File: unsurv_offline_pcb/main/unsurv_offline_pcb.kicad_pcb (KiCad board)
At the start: 4 copper layers, 35 x 50 mm, 51 parts, among them J1 USB_B_Micro, J2 S2B-PH-SM4-TB_LF__SN_, J3 1.27mm_female_connector, Q1 Q_PMOS_GSD, Q2 UMH3N, SW1 SW_DIP_x01, U1 MCP73831-2-OT, U2 APX803L20, U3 AP2112K-3.3, U4 MPU-6050_NRND, U5 ESP32-WROOM-32, U6 CAM-M8C-0-10, U7 CH340G

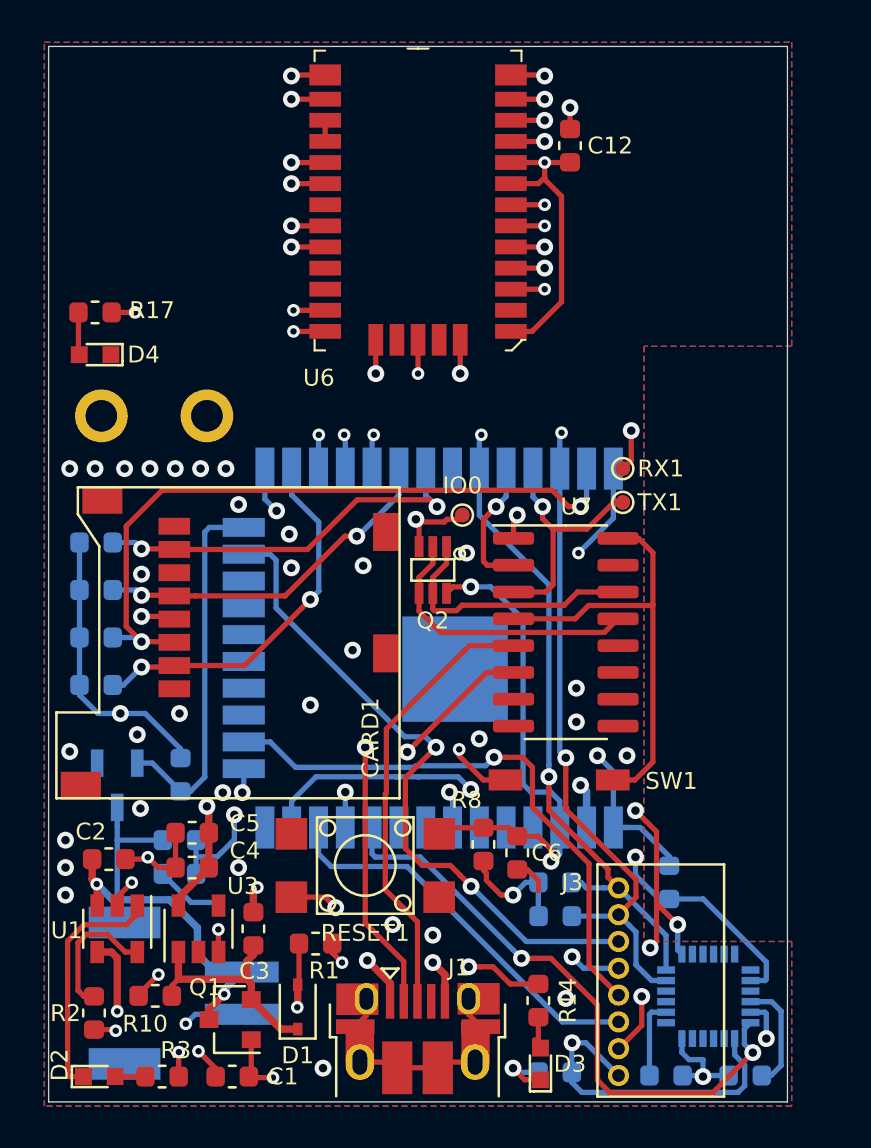
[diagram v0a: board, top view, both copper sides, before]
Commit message: added 3x2 pads for pogo pins
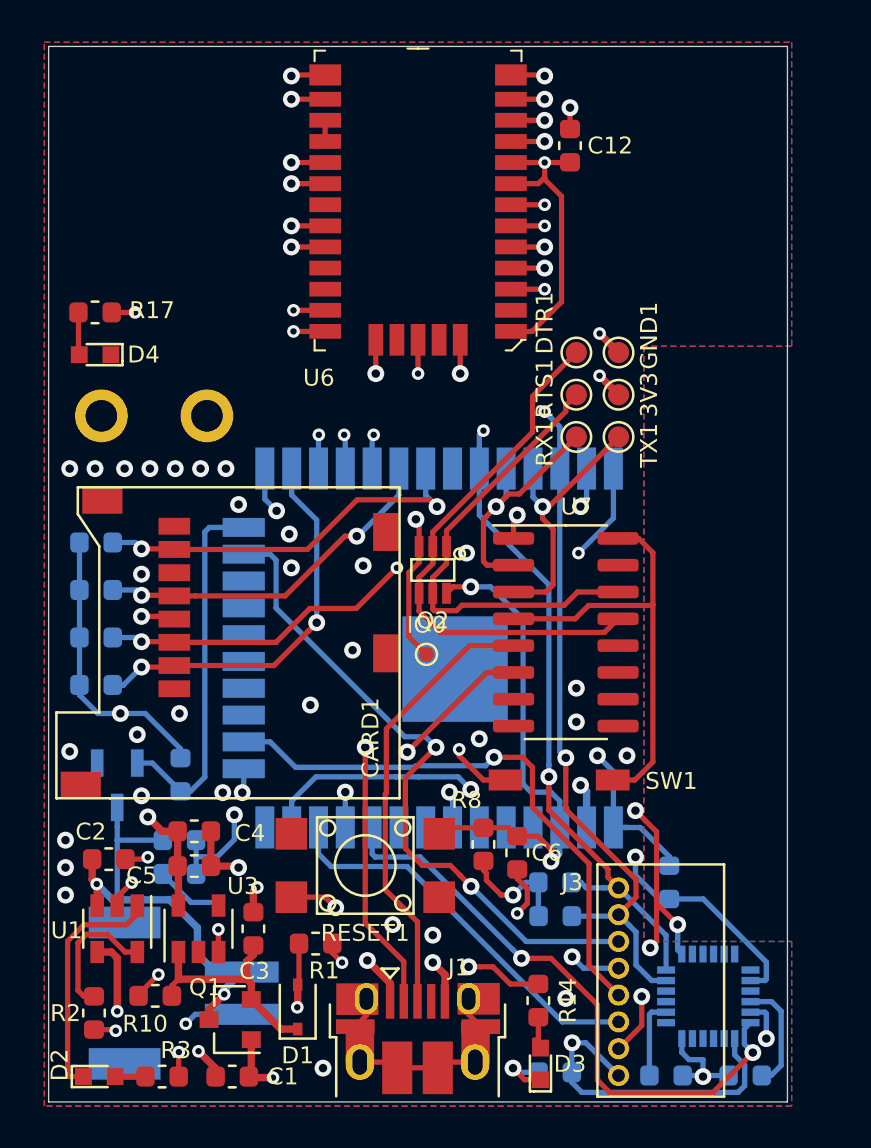
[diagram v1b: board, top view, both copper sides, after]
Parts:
- added 3V3: TestPoint, TestPoint:TestPoint_Pad_D1.0mm, F.Cu at (102.0, 91.5)
- added DTR1: TestPoint, TestPoint:TestPoint_Pad_D1.0mm, F.Cu at (100.0, 89.5)
- added GND1: TestPoint, TestPoint:TestPoint_Pad_D1.0mm, F.Cu at (102.0, 89.5)
- added RTS1: TestPoint, TestPoint:TestPoint_Pad_D1.0mm, F.Cu at (100.0, 91.5)
- RX1, TX1: footprint unsurv_offline_pcb_footprints:TestPoint_Pad_D0.7mm -> TestPoint:TestPoint_Pad_D1.0mm
- moved IO0 6.82 mm to (92.9, 103.8)
- moved TX1 3.11 mm to (102.0, 93.5), turned to 270 degrees
- moved RX1 2.66 mm to (100.0, 93.5), turned to 90 degrees
- moved C4 1.72 mm to (81.9, 112.2), turned to 180 degrees
- moved C5 1.58 mm to (81.9, 113.8), turned to 180 degrees
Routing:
- net DTR: track 13.4 -> 25.4 mm
- net RTS: track 12.4 -> 22.1 mm
- net 23: track 33.3 -> 26.8 mm, vias 2 -> 3
- net SDA: track 46.7 -> 41.1 mm
- net RX0: track 16.2 -> 11.5 mm, vias 2 -> 1
- net 5: track 30.0 -> 25.6 mm
- net SCL: track 47.4 -> 43.8 mm
- net 0: track 12.7 -> 16.0 mm
- net GND: track 84.4 -> 86.1 mm, vias 67 -> 69
- net +3V3: track 72.1 -> 73.6 mm, vias 9 -> 10
- net TX0: track 11.9 -> 12.9 mm
- net 4: track 17.9 -> 18.7 mm

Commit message: added RF430CL330H to pcb
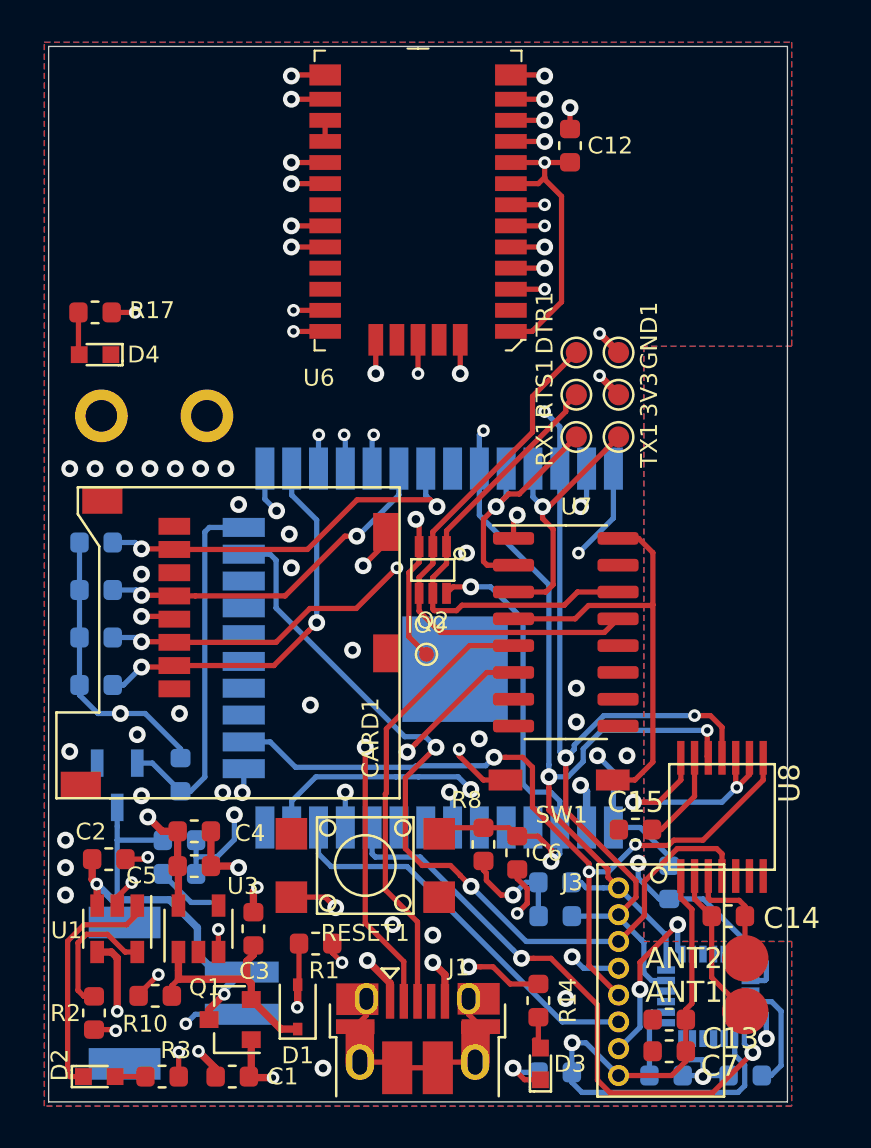
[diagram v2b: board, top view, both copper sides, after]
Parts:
- added ANT1: TestPoint, unsurv_offline_pcb_footprints:PogoPin_2_2mm_circular, F.Cu at (108.0, 120.7)
- added ANT2: TestPoint, unsurv_offline_pcb_footprints:PogoPin_2_2mm_circular, F.Cu at (108.0, 118.2)
- added C13: 1yF, Capacitor_SMD:C_0603_1608Metric, F.Cu at (104.4, 121.1)
- added C14: 10pF, Capacitor_SMD:C_0603_1608Metric, F.Cu at (107.2, 116.2)
- added C15: 470nF, Capacitor_SMD:C_0603_1608Metric, F.Cu at (102.8, 112.1)
- added C7: 0.1yF, Capacitor_SMD:C_0603_1608Metric, F.Cu at (104.4, 122.6)
- added U8: RF430CL330H, unsurv_offline_pcb_footprints:RF430CL330H, F.Cu at (106.9, 111.5)
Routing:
- net +3V3: track 73.6 -> 86.0 mm
- net 13: track 27.1 -> 38.2 mm, vias 1 -> 3
- net SDA: track 41.1 -> 51.3 mm, vias 3 -> 4
- net SCL: track 43.8 -> 53.8 mm, vias 3 -> 4
- net GND: track 86.1 -> 95.8 mm
- net 15: track 31.6 -> 40.4 mm
- net ANT1: track 0.00 -> 7.39 mm
- net ANT2: track 0.00 -> 5.42 mm
- net Net-(C15-Pad1): track 0.00 -> 4.49 mm

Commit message: bottom case
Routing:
- net GND: track 95.8 -> 101.1 mm, vias 69 -> 70
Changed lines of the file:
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@@
     (thickness 1.6)
     (drawings 4)
-    (tracks 761)
+    (tracks 768)
     (zones 0)
     (modules 62)
@@
   (module unsurv_offline_pcb_footprints:RF430CL330H (layer F.Cu)
     (at 106.9 111.5 90)
-    (fp_text reference U8 (at 1.6 3.2 90) (layer F.SilkS)
-      (effects (font (size 1 1) (thickness 0.15)))
+    (fp_text reference U8 (at 4.6 1.2 180) (layer F.SilkS)
+      (effects (font (size 0.8 0.8) (thickness 0.1)))
     )
     (fp_text value RF430CL330H (at 0 5.3 90) (layer F.Fab)
@@
     (attr smd)
     (fp_text reference C15 (at 0 1.3) (layer F.SilkS)
-      (effects (font (size 1 1) (thickness 0.15)))
+      (effects (font (size 0.8 0.8) (thickness 0.1)))
     )
     (fp_text value 470nF (at 0 1.43) (layer F.Fab)
@@
     )
     (fp_text user %R (at 0 0) (layer F.Fab)
-      (effects (font (size 0.4 0.4) (thickness 0.06)))
+      (effects (font (size 1 1) (thickness 0.15)))
     )
     (fp_line (start 1.48 0.73) (end -1.48 0.73) (layer F.CrtYd) (width 0.05))
@@
     (tags capacitor)
     (attr smd)
-    (fp_text reference C14 (at 3 0.1) (layer F.SilkS)
-      (effects (font (size 1 1) (thickness 0.15)))
+    (fp_text reference C14 (at -3 0.1) (layer F.SilkS)
+      (effects (font (size 0.8 0.8) (thickness 0.1)))
     )
     (fp_text value 10pF (at 0 1.43) (layer F.Fab)
@@
     )
     (fp_text user %R (at 0 0) (layer F.Fab)
-      (effects (font (size 0.4 0.4) (thickness 0.06)))
+      (effects (font (size 1 1) (thickness 0.15)))
     )
     (fp_line (start 1.48 0.73) (end -1.48 0.73) (layer F.CrtYd) (width 0.05))
@@
     (attr smd)
     (fp_text reference C13 (at -2.9 -0.9) (layer F.SilkS)
-      (effects (font (size 1 1) (thickness 0.15)))
+      (effects (font (size 0.8 0.8) (thickness 0.1)))
     )
     (fp_text value 1yF (at 0 1.43) (layer F.Fab)
@@
     )
     (fp_text user %R (at 0 0) (layer F.Fab)
-      (effects (font (size 0.4 0.4) (thickness 0.06)))
+      (effects (font (size 1 1) (thickness 0.15)))
     )
     (fp_line (start 1.48 0.73) (end -1.48 0.73) (layer F.CrtYd) (width 0.05))
@@
     (attr smd)
     (fp_text reference C7 (at -2.4 -0.7) (layer F.SilkS)
-      (effects (font (size 1 1) (thickness 0.15)))
+      (effects (font (size 0.8 0.8) (thickness 0.1)))
     )
     (fp_text value 0.1yF (at 0 1.43) (layer F.Fab)
@@
     )
     (fp_text user %R (at 0 0) (layer F.Fab)
-      (effects (font (size 0.4 0.4) (thickness 0.06)))
+      (effects (font (size 1 1) (thickness 0.15)))
     )
     (fp_line (start 1.48 0.73) (end -1.48 0.73) (layer F.CrtYd) (width 0.05))
@@
     (at 108 118.2 270)
     (fp_text reference ANT2 (at 0 2.9 180) (layer F.SilkS)
-      (effects (font (size 1 1) (thickness 0.15)))
+      (effects (font (size 0.8 0.8) (thickness 0.1)))
     )
     (fp_text value TestPoint (at 0 5.25 90) (layer F.Fab)
@@
     (at 108 120.7 270)
     (fp_text reference ANT1 (at -0.9 2.9 180) (layer F.SilkS)
-      (effects (font (size 1 1) (thickness 0.15)))
+      (effects (font (size 0.8 0.8) (thickness 0.1)))
     )
     (fp_text value TestPoint (at 0 5.25 90) (layer F.Fab)
@@
   (module unsurv_offline_pcb_footprints:UMH3N (layer F.Cu)
     (at 93.2 99.8 180)
-    (fp_text reference Q2 (at 0 -2.4) (layer F.SilkS)
+    (fp_text reference Q2 (at -1.4 2.3) (layer F.SilkS)
       (effects (font (size 0.8 0.8) (thickness 0.1)))
     )
@@
   (segment (start 90.975 98.525) (end 89.9 99.6) (width 0.25) (layer F.Cu) (net 1))
   (segment (start 90.975 98) (end 90.975 98.525) (width 0.25) (layer F.Cu) (net 1))
+  (via (at 99.086635 121.727633) (size 0.6) (drill 0.3) (layers F.Cu B.Cu) (net 1))
+  (segment (start 99.5 120.1) (end 99.5 121.314268) (width 0.25) (layer F.Cu) (net 1))
+  (segment (start 99.5 121.314268) (end 99.086635 121.727633) (width 0.25) (layer F.Cu) (net 1))
+  (segment (start 99.386634 121.427634) (end 99.086635 121.727633) (width 0.25) (layer B.Cu) (net 1))
+  (segment (start 100.947634 121.427634) (end 99.386634 121.427634) (width 0.25) (layer B.Cu) (net 1))
+  (segment (start 102 122.48) (end 100.947634 121.427634) (width 0.25) (layer B.Cu) (net 1))
   (via (at 90.100006 118.3) (size 0.8) (drill 0.4) (layers F.Cu B.Cu) (net 2))
   (segment (start 91.175 119.374994) (end 91.175 120.235) (width 0.35) (layer F.Cu) (net 2))
@@
   (segment (start 96.050697 118.6) (end 95.465685 118.6) (width 0.25) (layer F.Cu) (net 66))
   (segment (start 98.2 119.4125) (end 96.863197 119.4125) (width 0.25) (layer F.Cu) (net 66))
-  (segment (start 99.336998 121.21) (end 91.977008 113.85001) (width 0.25) (layer B.Cu) (net 67))
-  (segment (start 102 121.21) (end 99.336998 121.21) (width 0.25) (layer B.Cu) (net 67))
+  (segment (start 101.59 120.8) (end 98.926998 120.8) (width 0.25) (layer B.Cu) (net 67))
+  (segment (start 102 121.21) (end 101.59 120.8) (width 0.25) (layer B.Cu) (net 67))
+  (segment (start 98.926998 120.8) (end 91.977008 113.85001) (width 0.25) (layer B.Cu) (net 67))
+  (segment (start 91.977008 113.85001) (end 88.38501 113.85001) (width 0.25) (layer B.Cu) (net 67))
   (segment (start 87.785 113.25) (end 87.785 112) (width 0.25) (layer B.Cu) (net 67))
   (segment (start 88.38501 113.85001) (end 87.785 113.25) (width 0.25) (layer B.Cu) (net 67))
-  (segment (start 91.977008 113.85001) (end 88.38501 113.85001) (width 0.25) (layer B.Cu) (net 67))
   (segment (start 103.575 120.75) (end 104.25 120.75) (width 0.25) (layer B.Cu) (net 68))
   (segment (start 103.564998 120.75) (end 103.575 120.75) (width 0.25) (layer B.Cu) (net 68))
